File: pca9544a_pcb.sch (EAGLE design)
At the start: 3 parts

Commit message: apply lib update
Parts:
- removed U$1: PCA9544ABS, mylib:PCA9544ABS
- added IC1: PCA9544ABS, mylib:PCA9544ABS
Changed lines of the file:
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@@
 <part name="GIT1" library="git-revision" deviceset="GIT-REVISION" device="_1.7"/>
 <part name="B1" library="mylib" deviceset="UNIVERSALBOARD" device="-45"/>
-<part name="U$1" library="mylib" deviceset="PCA9544A" device="BS"/>
+<part name="IC1" library="mylib" deviceset="PCA9544A" device="BS"/>
 </parts>
 <sheets>
@@
 <instance part="GIT1" gate="G$1" x="215.9" y="20.32"/>
 <instance part="B1" gate="G$1" x="165.1" y="7.62"/>
-<instance part="U$1" gate="G$1" x="93.98" y="86.36"/>
+<instance part="IC1" gate="G$1" x="109.22" y="81.28"/>
 </instances>
 <busses>

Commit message: add submodules
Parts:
- removed B1: UNIVERSALBOARD-45, mylib:UNIVERSALBOARD-45
- added C1: (no value), mylib:C-SMD-0.1U-1608
- added P1, P2, P3, P4: (no value), mylib:PCB-CORNER
- added R1, R10, R11, R12, R13, R14, R15, R16, R17, R18, R2, R3, R4, R5, R6, R7, R8, R9: (no value), mylib:R-US-10K-1608
- added R19, R20, R21: (no value), mylib:R-US--1005SHORT
- added X1, X2, X3, X4, X5: TSW-104-02-S-S, con-samtec.local:TSW-104-02-S-S
- GIT1: value (none) -> 26910e7; device git-revision:GIT-REVISION_1.7 -> git-revision:GIT-REVISION_1.2
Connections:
- new net GND: C1.2, IC1.GND, R19.1, R20.1, R21.1, X1-4.1, X2-4.1, X3-4.1, X4-4.1, X5-4.1
- new net N$1: IC1.A2, R1.1, R19.2
- new net N$10: IC1.SCL1, R14.1, X3-3.1
- new net N$11: IC1.SDA1, R13.1, X3-2.1
- new net N$12: IC1.!INT1!, R8.1
- new net N$13: IC1.SCL2, R16.1, X4-3.1
- new net N$14: IC1.SDA2, R15.1, X4-2.1
- new net N$15: IC1.!INT2!, R9.1
- new net N$16: IC1.SCL3, R18.1, X5-3.1
- new net N$17: IC1.SDA3, R17.1, X5-2.1
- new net N$18: IC1.!INT3!, R10.1
- new net N$19: R11.2, R12.2, X2-1.1
- new net N$2: IC1.A1, R2.1, R20.2
- new net N$20: R13.2, R14.2, X3-1.1
- new net N$21: R15.2, R16.2, X4-1.1
- new net N$22: R17.2, R18.2, X5-1.1
- new net N$3: IC1.A0, R21.2, R3.1
- new net N$4: IC1.SCL, R4.1, X1-3.1
- new net N$5: IC1.SDA, R5.1, X1-2.1
- new net N$6: IC1.!INT!, R6.1
- new net N$7: IC1.SCL0, R12.1, X2-3.1
- new net N$8: IC1.SDA0, R11.1, X2-2.1
- new net N$9: IC1.!INT0!, R7.1
- new net VCC: C1.1, IC1.VDD, R1.2, R10.2, R2.2, R3.2, R4.2, R5.2, R6.2, R7.2, R8.2, R9.2, X1-1.1
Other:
- note added: "R1-3 Not mounted R4-10 10K R11-21 Not mounted --- R1-3 and R19-21 are slave address selector Cut shorting circuit when mount R1-3 --- X1-5 I2C connectors are GROVE INCOMPATIBLE --- interrupt input/output is unused --- slave bus SDA/SCL pulled up to each slave bus VDD"
- moved on the sheet: IC1

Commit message: gerber out
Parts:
- GIT1: value 26910e7 -> 61667e5
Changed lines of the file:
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@@
 <parts>
 <part name="FRAME1" library="frames" deviceset="A4L-LOC" device=""/>
-<part name="GIT1" library="git-revision" deviceset="GIT-REVISION" device="_1.2" value="26910e7"/>
+<part name="GIT1" library="git-revision" deviceset="GIT-REVISION" device="_1.2" value="61667e5"/>
 <part name="IC1" library="mylib" deviceset="PCA9544A" device="BS"/>
 <part name="R1" library="mylib" deviceset="R-US-*" device="-1608" technology="10K"/>

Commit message: replace X1-X5 to JST XH 4P right angle headers
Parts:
- X1, X2, X3, X4, X5: value TSW-104-02-S-S -> (none); device con-samtec.local:TSW-104-02-S-S -> mylib:S4B-XH-A
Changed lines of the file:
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@@
 <part name="SUPPLY1" library="mylib" deviceset="GND" device=""/>
 <part name="P+1" library="mylib" deviceset="VCC" device=""/>
-<part name="X1" library="con-samtec.local" deviceset="TSW-104-02-S-S" device=""/>
-<part name="X2" library="con-samtec.local" deviceset="TSW-104-02-S-S" device=""/>
-<part name="X3" library="con-samtec.local" deviceset="TSW-104-02-S-S" device=""/>
-<part name="X4" library="con-samtec.local" deviceset="TSW-104-02-S-S" device=""/>
-<part name="X5" library="con-samtec.local" deviceset="TSW-104-02-S-S" device=""/>
+<part name="X1" library="mylib" deviceset="S4B-XH-A" device=""/>
+<part name="X2" library="mylib" deviceset="S4B-XH-A" device=""/>
+<part name="X3" library="mylib" deviceset="S4B-XH-A" device=""/>
+<part name="X4" library="mylib" deviceset="S4B-XH-A" device=""/>
+<part name="X5" library="mylib" deviceset="S4B-XH-A" device=""/>
 <part name="P+2" library="mylib" deviceset="VCC" device=""/>
 <part name="P+3" library="mylib" deviceset="VCC" device=""/>

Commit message: gerber out
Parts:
- GIT1: value 61667e5 -> 3d5507e
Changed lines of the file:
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@@
 <parts>
 <part name="FRAME1" library="frames" deviceset="A4L-LOC" device=""/>
-<part name="GIT1" library="git-revision" deviceset="GIT-REVISION" device="_1.2" value="61667e5"/>
+<part name="GIT1" library="git-revision" deviceset="GIT-REVISION" device="_1.2" value="3d5507e"/>
 <part name="IC1" library="mylib" deviceset="PCA9544A" device="BS"/>
 <part name="R1" library="mylib" deviceset="R-US-*" device="-1608" technology="10K"/>

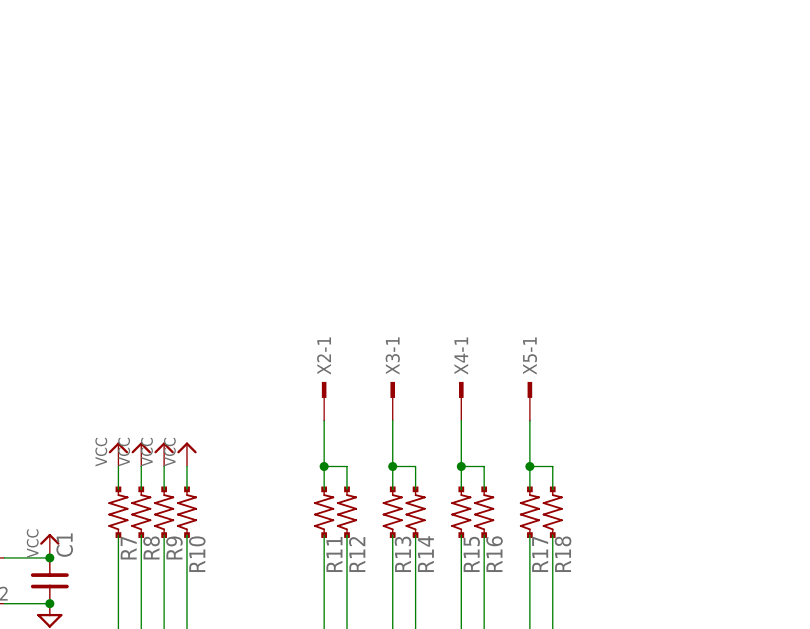
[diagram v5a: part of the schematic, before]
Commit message: add X6~X9 to short Host VDD and each channel VDD
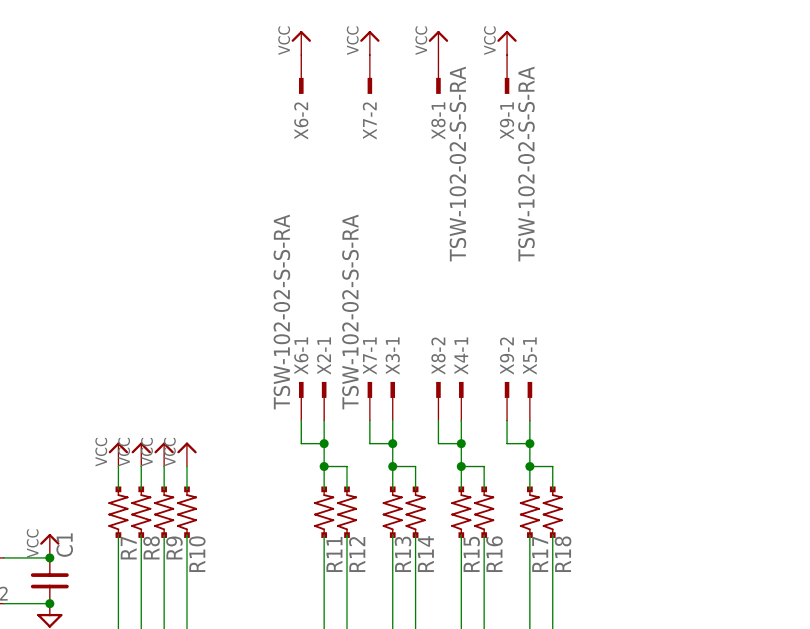
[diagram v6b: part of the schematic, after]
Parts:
- added X6, X7, X8, X9: TSW-102-02-S-S-RA, con-samtec.local:TSW-102-02-S-S-RA
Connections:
- net N$19: now also X6-1.1
- net N$20: now also X7-1.1
- net N$21: now also X8-2.1
- net N$22: now also X9-2.1
- net VCC: now also X6-2.1, X7-2.1, X8-1.1, X9-1.1
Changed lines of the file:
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@@
 <part name="P3" library="mylib" deviceset="PCB-CORNER" device=""/>
 <part name="P4" library="mylib" deviceset="PCB-CORNER" device=""/>
+<part name="X6" library="con-samtec.local" deviceset="TSW-102-02-S-S" device="-RA"/>
+<part name="X7" library="con-samtec.local" deviceset="TSW-102-02-S-S" device="-RA"/>
+<part name="X8" library="con-samtec.local" deviceset="TSW-102-02-S-S" device="-RA"/>
+<part name="X9" library="con-samtec.local" deviceset="TSW-102-02-S-S" device="-RA"/>
+<part name="P+13" library="mylib" deviceset="VCC" device=""/>
+<part name="P+14" library="mylib" deviceset="VCC" device=""/>
+<part name="P+15" library="mylib" deviceset="VCC" device=""/>
+<part name="P+16" library="mylib" deviceset="VCC" device=""/>
 </parts>
 <sheets>
@@
 <instance part="P3" gate="G$1" x="144.78" y="17.78" rot="R180"/>
 <instance part="P4" gate="G$1" x="144.78" y="12.7" rot="R270"/>
+<instance part="X6" gate="-1" x="139.7" y="129.54" rot="R90"/>
+<instance part="X6" gate="-2" x="139.7" y="165.1" rot="R270"/>
+<instance part="X7" gate="-1" x="147.32" y="129.54" rot="R90"/>
+<instance part="X7" gate="-2" x="147.32" y="165.1" rot="R270"/>
+<instance part="P+13" gate="VCC" x="139.7" y="170.18"/>
+<instance part="P+14" gate="VCC" x="147.32" y="170.18"/>
+<instance part="P+15" gate="VCC" x="154.94" y="170.18"/>
+<instance part="P+16" gate="VCC" x="162.56" y="170.18"/>
+<instance part="X8" gate="-2" x="154.94" y="129.54" rot="R90"/>
+<instance part="X8" gate="-1" x="154.94" y="165.1" rot="R270"/>
+<instance part="X9" gate="-2" x="162.56" y="129.54" rot="R90"/>
+<instance part="X9" gate="-1" x="162.56" y="165.1" rot="R270"/>
 </instances>
 <busses>
@@
 <pinref part="R10" gate="G$1" pin="2"/>
 </segment>
+<segment>
+<pinref part="X6" gate="-2" pin="1"/>
+<pinref part="P+13" gate="VCC" pin="VCC"/>
+</segment>
+<segment>
+<pinref part="X7" gate="-2" pin="1"/>
+<pinref part="P+14" gate="VCC" pin="VCC"/>
+</segment>
+<segment>
+<pinref part="P+15" gate="VCC" pin="VCC"/>
+<pinref part="X8" gate="-1" pin="1"/>
+</segment>
+<segment>
+<pinref part="P+16" gate="VCC" pin="VCC"/>
+<pinref part="X9" gate="-1" pin="1"/>
+</segment>
 </net>
 <net name="N$19" class="0">
@@
 <wire x1="142.24" y1="121.92" x2="144.78" y2="121.92" width="0.1524" layer="91"/>
 <pinref part="X2" gate="-1" pin="1"/>
-<wire x1="142.24" y1="127" x2="142.24" y2="121.92" width="0.1524" layer="91"/>
+<wire x1="142.24" y1="127" x2="142.24" y2="124.46" width="0.1524" layer="91"/>
 <junction x="142.24" y="121.92"/>
+<wire x1="142.24" y1="124.46" x2="142.24" y2="121.92" width="0.1524" layer="91"/>
+<wire x1="142.24" y1="124.46" x2="139.7" y2="124.46" width="0.1524" layer="91"/>
+<junction x="142.24" y="124.46"/>
+<pinref part="X6" gate="-1" pin="1"/>
+<wire x1="139.7" y1="124.46" x2="139.7" y2="127" width="0.1524" layer="91"/>
 </segment>
 </net>
@@
 <wire x1="149.86" y1="121.92" x2="152.4" y2="121.92" width="0.1524" layer="91"/>
 <pinref part="X3" gate="-1" pin="1"/>
-<wire x1="149.86" y1="121.92" x2="149.86" y2="127" width="0.1524" layer="91"/>
+<wire x1="149.86" y1="121.92" x2="149.86" y2="124.46" width="0.1524" layer="91"/>
 <junction x="149.86" y="121.92"/>
+<wire x1="149.86" y1="124.46" x2="149.86" y2="127" width="0.1524" layer="91"/>
+<wire x1="149.86" y1="124.46" x2="147.32" y2="124.46" width="0.1524" layer="91"/>
+<junction x="149.86" y="124.46"/>
+<pinref part="X7" gate="-1" pin="1"/>
+<wire x1="147.32" y1="124.46" x2="147.32" y2="127" width="0.1524" layer="91"/>
 </segment>
 </net>
@@
 <wire x1="157.48" y1="121.92" x2="160.02" y2="121.92" width="0.1524" layer="91"/>
 <pinref part="X4" gate="-1" pin="1"/>
-<wire x1="157.48" y1="127" x2="157.48" y2="121.92" width="0.1524" layer="91"/>
+<wire x1="157.48" y1="127" x2="157.48" y2="124.46" width="0.1524" layer="91"/>
 <junction x="157.48" y="121.92"/>
+<wire x1="157.48" y1="124.46" x2="157.48" y2="121.92" width="0.1524" layer="91"/>
+<wire x1="157.48" y1="124.46" x2="154.94" y2="124.46" width="0.1524" layer="91"/>
+<junction x="157.48" y="124.46"/>
+<wire x1="154.94" y1="124.46" x2="154.94" y2="127" width="0.1524" layer="91"/>
+<pinref part="X8" gate="-2" pin="1"/>
 </segment>
 </net>
@@
 <wire x1="165.1" y1="121.92" x2="167.64" y2="121.92" width="0.1524" layer="91"/>
 <pinref part="X5" gate="-1" pin="1"/>
-<wire x1="165.1" y1="121.92" x2="165.1" y2="127" width="0.1524" layer="91"/>
+<wire x1="165.1" y1="121.92" x2="165.1" y2="124.46" width="0.1524" layer="91"/>
 <junction x="165.1" y="121.92"/>
-</segment>
-</net>
+<wire x1="165.1" y1="124.46" x2="165.1" y2="127" width="0.1524" layer="91"/>
+<wire x1="165.1" y1="124.46" x2="162.56" y2="124.46" width="0.1524" layer="91"/>
+<junction x="165.1" y="124.46"/>
+<wire x1="162.56" y1="124.46" x2="162.56" y2="127" width="0.1524" layer="91"/>
+<pinref part="X9" gate="-2" pin="1"/>
+</segment>
+</net>

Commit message: fix silk
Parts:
- GIT1: value 3d5507e -> 4bf204c
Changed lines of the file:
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@@
 <parts>
 <part name="FRAME1" library="frames" deviceset="A4L-LOC" device=""/>
-<part name="GIT1" library="git-revision" deviceset="GIT-REVISION" device="_1.2" value="3d5507e"/>
+<part name="GIT1" library="git-revision" deviceset="GIT-REVISION" device="_1.2" value="4bf204c"/>
 <part name="IC1" library="mylib" deviceset="PCA9544A" device="BS"/>
 <part name="R1" library="mylib" deviceset="R-US-*" device="-1608" technology="10K"/>

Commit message: gerber out
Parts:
- GIT1: value 4bf204c -> adf3d9e
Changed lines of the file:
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@@
 <parts>
 <part name="FRAME1" library="frames" deviceset="A4L-LOC" device=""/>
-<part name="GIT1" library="git-revision" deviceset="GIT-REVISION" device="_1.2" value="4bf204c"/>
+<part name="GIT1" library="git-revision" deviceset="GIT-REVISION" device="_1.2" value="adf3d9e"/>
 <part name="IC1" library="mylib" deviceset="PCA9544A" device="BS"/>
 <part name="R1" library="mylib" deviceset="R-US-*" device="-1608" technology="10K"/>
